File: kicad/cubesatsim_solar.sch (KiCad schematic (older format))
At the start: 23 parts, among them J1 Sensor Inputs, J10 INA219 Sensor Board, J11 INA219 Sensor Board, J12 INA219 Sensor Board, J13 3.5mm TRS Audio Jack with 2 S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, J14 RBF connector, J2 Battery In/Out, J3 Vdc In, J4 Vout to MoPOWER, J5 RBF Switch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

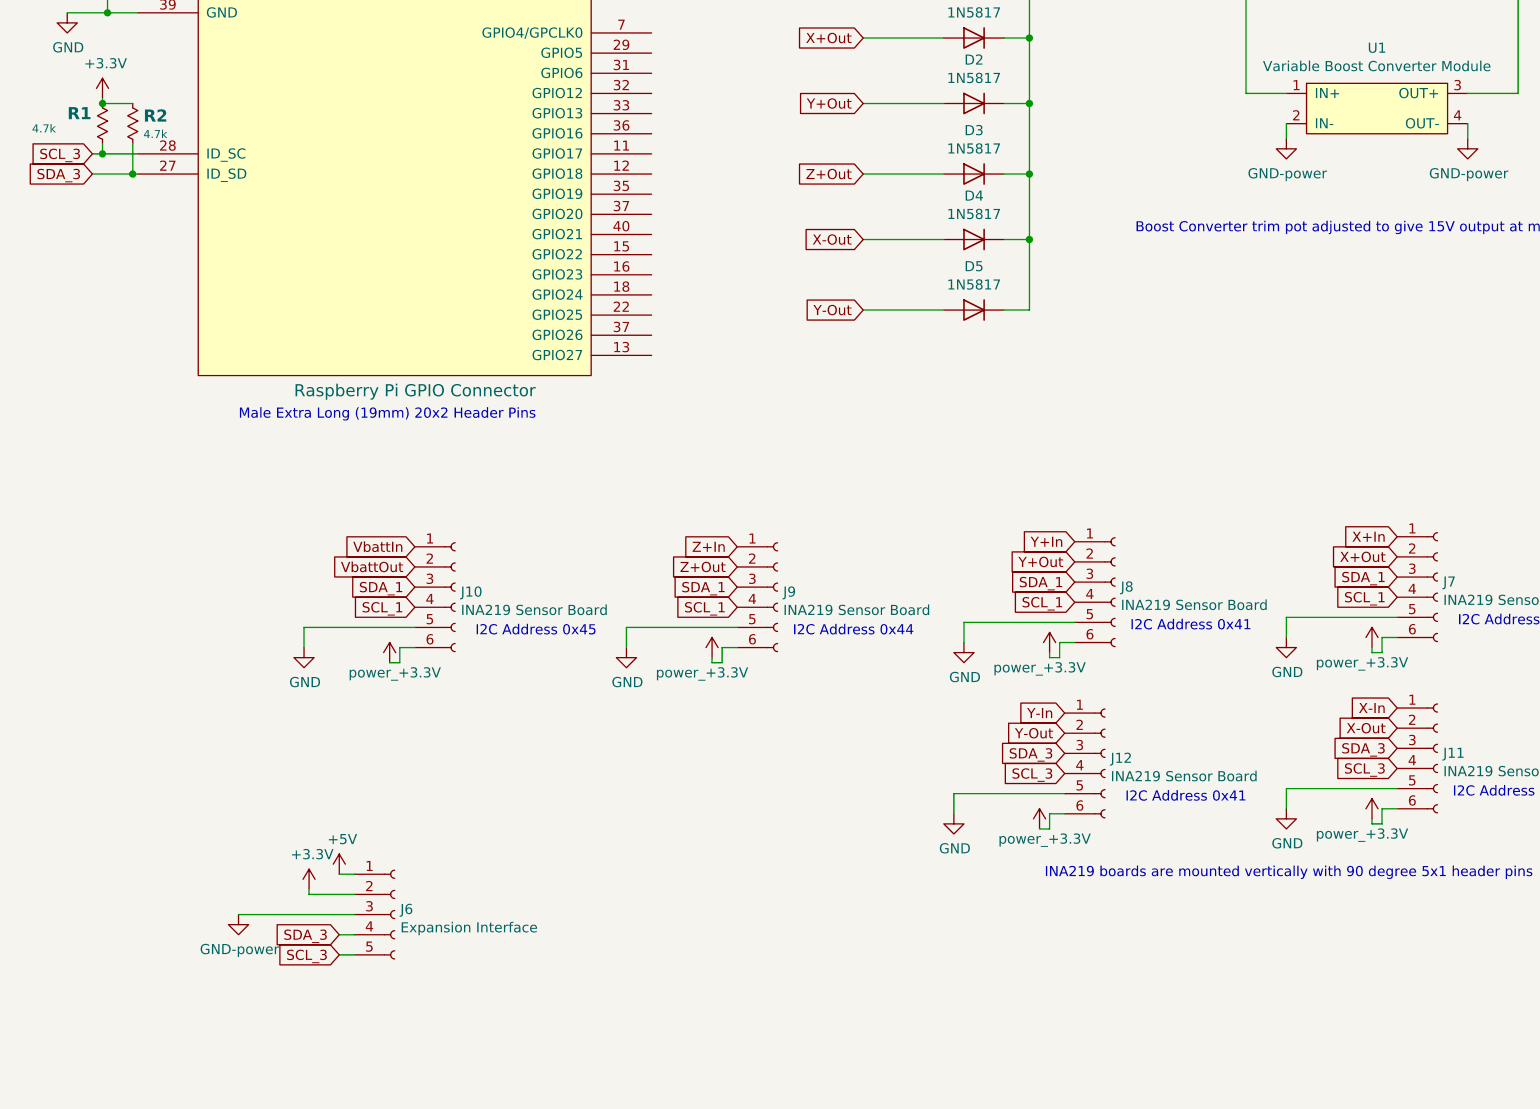
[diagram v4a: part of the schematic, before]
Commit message: Fixed I2C bus error
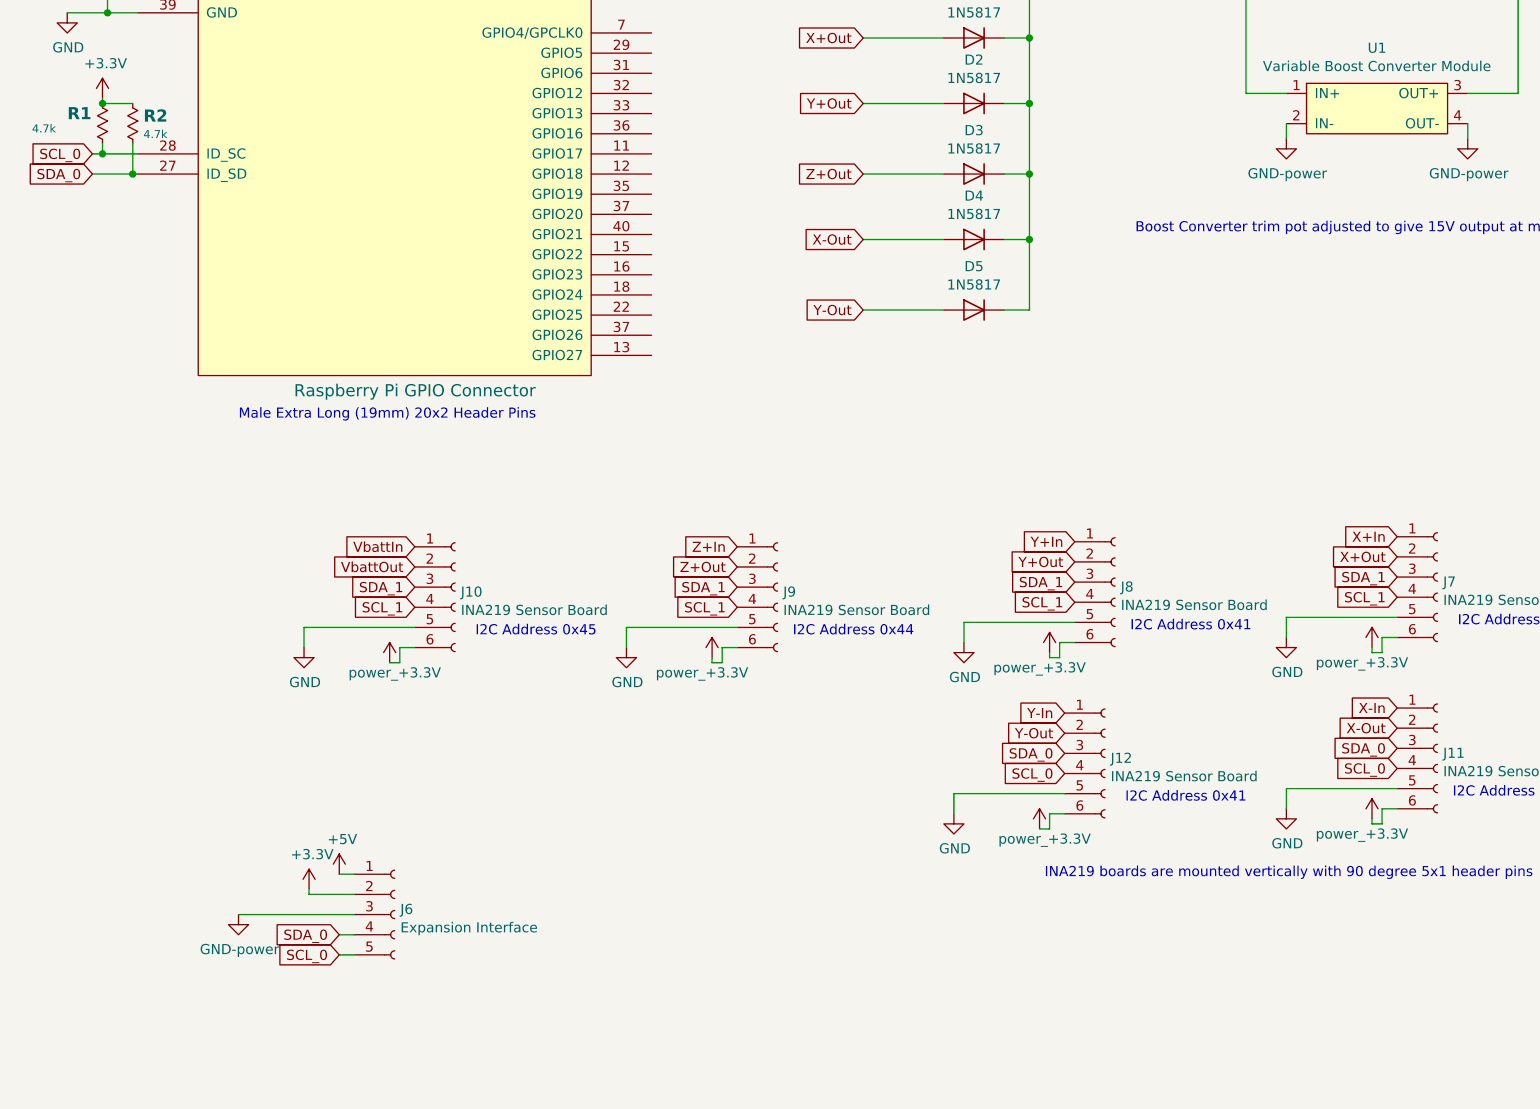
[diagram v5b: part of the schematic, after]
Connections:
- net SCL_3 renamed SCL_0
- net SDA_3 renamed SDA_0
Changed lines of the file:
@@
 Title "AMSAT CubeSat Simulator Solar Panel Board"
 Date "December 15, 2018"
-Rev "Beta1.2"
+Rev "Beta1.3"
 Comp "See https://github.com/alanbjohnston/cubesatsim"
 Comment1 "KU2Y"
@@
 	7325 5475 7325 5450
 Text GLabel 975  3100 0    50   Input ~ 0
-SDA_3
+SDA_0
 Text GLabel 975  3000 0    50   Input ~ 0
-SCL_3
+SCL_0
 $Comp
 L pihat_template-rescue:Raspberry_Pi_+_Conn-pihat_template-rescue P3
@@
 $EndComp
 Text GLabel 2200 6875 0    50   Input ~ 0
-SDA_3
+SDA_0
 Text GLabel 2200 6975 0    50   Input ~ 0
-SCL_3
+SCL_0
 Wire Wire Line
 	2275 6875 2200 6875
@@
 X-Out
 Text GLabel 7450 5950 0    50   Input ~ 0
-SDA_3
+SDA_0
 Text GLabel 7450 6050 0    50   Input ~ 0
-SCL_3
+SCL_0
 $Comp
 L pihat_template-rescue:GND-power #PWR0120
@@
 Y-Out
 Text GLabel 5800 5975 0    50   Input ~ 0
-SDA_3
+SDA_0
 Text GLabel 5800 6075 0    50   Input ~ 0
-SCL_3
+SCL_0
 $Comp
 L pihat_template-rescue:GND-power #PWR0122

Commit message: vB2 PCB Submitted to PCB Way
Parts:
- removed J13: 3.5mm TRS Audio Jack with 2 Switches, symbol pihat_template-rescue:Audio-Jack-3_2Switches-conn2
- removed J14: RBF connector, symbol pihat_template-rescue:Conn_01x05_Female-Connector
- removed U1: Variable Boost Converter Module, symbol pihat_template-rescue:BoostConverter-New_Library
- added J13: IN+, Connector_PinSocket_2.54mm:PinSocket_1x01_P2.54mm_Vertical, symbol pihat_template-rescue:CONN_01X01-conn2
- added J14: IN-, Connector_PinSocket_2.54mm:PinSocket_1x01_P2.54mm_Vertical, symbol pihat_template-rescue:CONN_01X01-conn2
- added J15: OUT+, Connector_PinSocket_2.54mm:PinSocket_1x01_P2.54mm_Vertical, symbol pihat_template-rescue:CONN_01X01-conn2
- added J16: OUT-, Connector_PinSocket_2.54mm:PinSocket_1x01_P2.54mm_Vertical, symbol pihat_template-rescue:CONN_01X01-conn2
- added J17: 35RAPC4BH3, 35RAPC4BH3:SWITCHCRAFT_35RAPC4BH3, symbol 35RAPC4BH3:35RAPC4BH3
- J3, J4: footprint Connector_PinHeader_2.54mm:PinHeader_1x02_P2.54mm_Vertical -> Connector_Wire:SolderWirePad_1x02_P3.81mm_Drill1.2mm
- P3: value Raspberry Pi GPIO Connector -> GPIO Male Extra Long (19mm) 20x2 Header Pins; footprint w_conn_strip:vasch_strip_20x2 -> Connector_PinHeader_2.54mm:PinHeader_2x20_P2.54mm_Vertical
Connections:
- net GND: now also J3.2 (P2), J14.1 (P1), J16.1 (P1)
- net at D1.1 (K), D2.1 (K), D3.1 (K)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: now also J17.3
- net at J5.2 (P2): now also J13.1 (P1), J17.2
- net at J5.3 (P3): now also J15.1 (P1), J17.4
- net at J4.1 (P1), J5.4 (P4): now also J17.5
- net at J3.1 (P1), J5.5 (P5): now also J17.1
- net SCL_0 renamed SCL_3
- net SDA_0 renamed SDA_3
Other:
- note added: "Boost Converter trim pot adjusted to \ngive 15V output at maximum solar \npanel voltage input."
- note added: "To Solar Panels"
- note added: "U1 Boost Converter"
- note added: "Use either J17 if RBF \nswitch is mounted on \nPC board, or J5 if RBF \nswitch is connected \nthrough wires on \nthe frame."
- note added: "With RBF switch inserted (3.5mm jack plugged in),\n Vout to MoPower comes from the Vdc in barrel jack\n through 3.5mm plug that has jumper between 3 and 1 \n(center and outer). Solar panels are isolated from the input to \nthe boost converter through the switch."
- note removed: "Boost Converter trim pot adjusted to give 15V output at maximum solar panel voltage input."
- note removed: "Male Extra Long (19mm) 20x2 Header Pins"
- note removed: "With RBF switch inserted (3.5mm jack plugged in), \nVout to MoPower comes from the Vdc in barrel jack\nthrough 3.5mm plug that has jumper between 3 and 1 \n(center and outer). Solar panels are isolated from the \ninput to the boost converter through the switch.\n"
- moved on the sheet: J10, J11, J3, J4

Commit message: kicad files for vB3 PCB
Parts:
- removed J1: Sensor Inputs, Connector_PinHeader_2.54mm:PinHeader_1x10_P2.54mm_Vertical, symbol pihat_template-rescue:Conn_01x10_Female-Connector
- removed J2: Battery In/Out, Connector_PinHeader_2.54mm:PinHeader_1x02_P2.54mm_Vertical, symbol pihat_template-rescue:CONN_01X02_FEMALE-conn2
- removed J3: Vdc In, Connector_Wire:SolderWirePad_1x02_P3.81mm_Drill1.2mm, symbol pihat_template-rescue:CONN_01X02-conn2
- removed J5: RBF Switch, Connector_PinHeader_2.54mm:PinHeader_1x05_P2.54mm_Vertical, symbol pihat_template-rescue:CONN_01X05-conn2
- added D6: 1N5817, Diode_THT:D_DO-41_SOD81_P3.81mm_Vertical_AnodeUp, symbol pihat_template-rescue:D-device
- added D7: LED, Diode_THT:D_DO-41_SOD81_P3.81mm_Vertical_AnodeUp, symbol pihat_template-rescue:D-device
- added J1: PJ-037AH, PJ-037AH:CUI_PJ-037AH, symbol PJ-037AH:PJ-037AH
- added J13: INA219 Sensor Board, Connector_PinHeader_2.54mm:PinHeader_1x06_P2.54mm_Vertical, symbol pihat_template-rescue:Conn_01x06_Female-Connector
- added J2: CONN_01X14, Connector_PinSocket_2.54mm:PinSocket_1x14_P2.54mm_Vertical, symbol conn2:CONN_01X14
- added R3: 220, Resistor_THT:R_Axial_DIN0207_L6.3mm_D2.5mm_P5.08mm_Vertical, symbol pihat_template-rescue:RESISTOR-passive
- J4: footprint Connector_Wire:SolderWirePad_1x02_P3.81mm_Drill1.2mm -> Connector_PinSocket_2.54mm:PinSocket_2x01_P2.54mm_Vertical
- renumbered J13 to J17, J17 to J3
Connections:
- net +3V3: now also J13.6 (Pin_6), R3.1
- net GND: now also J1.2, J13.5 (Pin_5), J2.10 (P10), J2.12 (P12), J2.14 (P14), J2.2 (P2), J2.4 (P4), J2.6 (P6)
- net SCL_3: now also J13.4 (Pin_4)
- net SDA_3: now also J13.3 (Pin_3)
- net VbattIn: now also J2.7 (P7)
- net VbattOut: now also J2.8 (P8)
- net at P3.11 (GPIO17): now also D7.1 (K)
- net at D1.1 (K), D2.1 (K), D3.1 (K)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: now also D6.1 (K)
- net at J3.1: now also J1.1
- net X+In renamed +X_In
- net +X_In: now also J2.1 (P1)
- net X+Out renamed +X_Out
- net X-In renamed -X_In
- net -X_In: now also J2.9 (P9)
- net X-Out renamed -X_Out
- net Y+In renamed +Y_In
- net +Y_In: now also J2.3 (P3)
- net Y+Out renamed +Y_Out
- net Y-In renamed -Y_In
- net -Y_In: now also J2.11 (P11)
- net Y-Out renamed -Y_Out
- net Z+In renamed +Z_In
- net +Z_In: now also J2.5 (P5)
- net Z+Out renamed +Z_Out
- new net: D7.2 (A), R3.2
- new net -Z_In: J13.1 (Pin_1), J2.13 (P13)
- new net -Z_Out: D6.2 (A), J13.2 (Pin_2)
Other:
- note added: "5.5mm x 2.1mm"
- note added: "I2C Address 0x44"
- note added: "INA219 boards are mounted vertically with 90 degree 1x6 header pins"
- note added: "RBF switch is mounted on \nPC board.\n"
- note removed: "Between NiMH battery and MoPower Board"
- note removed: "INA219 boards are mounted vertically with 90 degree 5x1 header pins"
- note removed: "To 5.5mm x 2.1mm"
- note removed: "Use either J17 if RBF \nswitch is mounted on \nPC board, or J5 if RBF \nswitch is connected \nthrough wires on \nthe frame."
